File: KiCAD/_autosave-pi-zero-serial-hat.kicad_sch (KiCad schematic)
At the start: 44 parts, among them J1 Conn_02x20_Counter_Clockwise, J2 Conn_01x02_Pin, J4 Screw_Terminal_01x04, Q1 AO3401A, Q2 MMBT5401, Q3 MMBT5401, U1 MAX13487EESA+, U2 TPS5430DDA

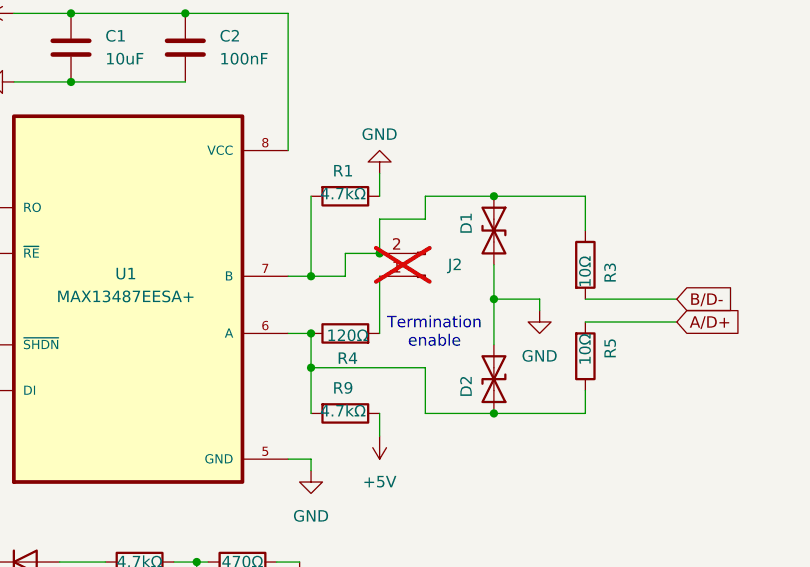
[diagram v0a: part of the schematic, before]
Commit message: Updated layout to fit on a single sided zero form factor board
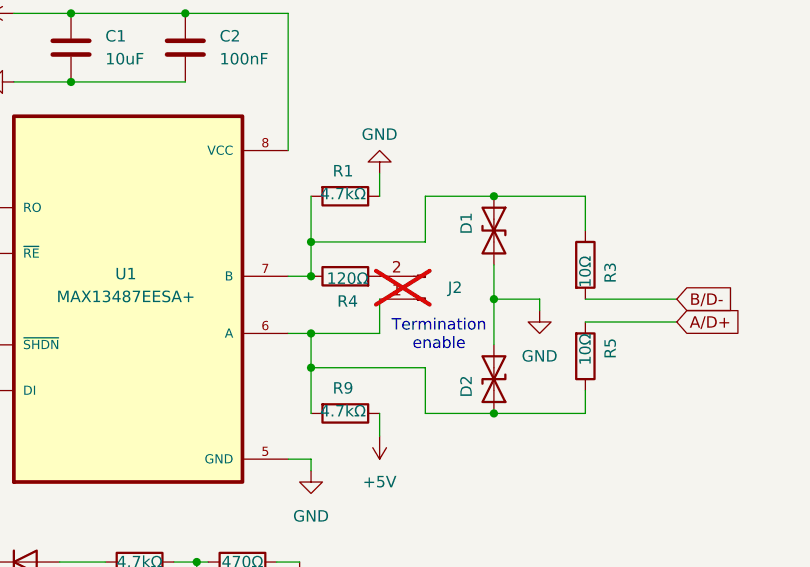
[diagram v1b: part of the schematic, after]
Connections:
- net at J2.1 (Pin_1): now also D2.1 (A1), R5.1, R9.2, U1.6 (A); no longer R4.2
- net at D1.1 (A1), R1.2, R3.1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: now also R4.1; no longer J2.2 (Pin_2)
- new net: J2.2 (Pin_2), R4.2
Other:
- moved on the sheet: J2, R4
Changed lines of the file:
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@@
 	)
 	(junction
-		(at 29.21 127)
-		(diameter 0)
-		(color 0 0 0 0)
-	)
-	(junction
-		(at 106.68 62.23)
+		(at 146.05 45.72)
 		(diameter 0)
 		(color 0 0 0 0)
 	)
 	(junction
-		(at 153.67 46.99)
+		(at 29.21 127)
 		(diameter 0)
 		(color 0 0 0 0)
 	)
 	(junction
-		(at 146.05 55.88)
+		(at 106.68 62.23)
 		(diameter 0)
 		(color 0 0 0 0)
@@
 	)
 	(junction
-		(at 146.05 49.53)
-		(diameter 0)
-		(color 0 0 0 0)
-	)
-	(junction
 		(at 95.25 127)
 		(diameter 0)
@@
 	)
 	(junction
+		(at 146.05 49.53)
+		(diameter 0)
+		(color 0 0 0 0)
+	)
+	(junction
 		(at 107.95 127)
 		(diameter 0)
@@
 		(color 0 0 0 0)
 	)
+	(junction
+		(at 146.05 55.88)
+		(diameter 0)
+		(color 0 0 0 0)
+	)
 	(no_connect
 		(at 43.18 55.88)
@@
 	(wire
 		(pts
-			(xy 149.86 49.53) (xy 149.86 46.99)
-		)
-		(stroke
-			(width 0)
-			(type default)
-		)
-	)
-	(wire
-		(pts
-			(xy 153.67 43.18) (xy 158.75 43.18)
-		)
-		(stroke
-			(width 0)
-			(type default)
-		)
-	)
-	(wire
-		(pts
 			(xy 107.95 127) (xy 107.95 128.27)
 		)
@@
 	(wire
 		(pts
-			(xy 158.75 43.18) (xy 158.75 40.64)
+			(xy 39.37 127) (xy 52.07 127)
 		)
 		(stroke
@@
 	(wire
 		(pts
-			(xy 39.37 127) (xy 52.07 127)
+			(xy 241.3 40.64) (xy 241.3 50.8)
 		)
 		(stroke
@@
 	(wire
 		(pts
-			(xy 241.3 40.64) (xy 241.3 50.8)
+			(xy 158.75 59.69) (xy 158.75 64.77)
 		)
 		(stroke
@@
 	(wire
 		(pts
-			(xy 158.75 59.69) (xy 158.75 64.77)
+			(xy 105.41 41.91) (xy 107.95 41.91)
 		)
 		(stroke
@@
 	(wire
 		(pts
-			(xy 105.41 41.91) (xy 107.95 41.91)
+			(xy 158.75 40.64) (xy 166.37 40.64)
 		)
 		(stroke
@@
 	(wire
 		(pts
-			(xy 158.75 40.64) (xy 166.37 40.64)
+			(xy 146.05 55.88) (xy 153.67 55.88)
 		)
 		(stroke
@@
 	(wire
 		(pts
+			(xy 153.67 52.07) (xy 153.67 55.88)
+		)
+		(stroke
+			(width 0)
+			(type default)
+		)
+	)
+	(wire
+		(pts
 			(xy 166.37 52.07) (xy 171.45 52.07)
 		)
@@
 	(wire
 		(pts
-			(xy 146.05 49.53) (xy 149.86 49.53)
+			(xy 146.05 45.72) (xy 158.75 45.72)
 		)
 		(stroke
@@
 	(wire
 		(pts
-			(xy 146.05 40.64) (xy 146.05 49.53)
-		)
-		(stroke
-			(width 0)
-			(type default)
-		)
-	)
-	(wire
-		(pts
-			(xy 153.67 49.53) (xy 153.67 55.88)
+			(xy 146.05 40.64) (xy 146.05 45.72)
 		)
 		(stroke
@@
 	(wire
 		(pts
-			(xy 149.86 46.99) (xy 153.67 46.99)
+			(xy 97.79 41.91) (xy 96.52 41.91)
 		)
 		(stroke
@@
 	(wire
 		(pts
-			(xy 97.79 41.91) (xy 96.52 41.91)
+			(xy 29.21 127) (xy 39.37 127)
 		)
 		(stroke
@@
 	(wire
 		(pts
-			(xy 29.21 127) (xy 39.37 127)
+			(xy 29.21 137.16) (xy 29.21 139.7)
 		)
 		(stroke
@@
 	(wire
 		(pts
-			(xy 29.21 137.16) (xy 29.21 139.7)
+			(xy 130.81 91.44) (xy 133.35 91.44)
 		)
 		(stroke
@@
 	(wire
 		(pts
-			(xy 130.81 91.44) (xy 133.35 91.44)
+			(xy 113.03 20.32) (xy 119.38 20.32)
 		)
 		(stroke
@@
 	(wire
 		(pts
-			(xy 113.03 20.32) (xy 119.38 20.32)
+			(xy 93.98 62.23) (xy 97.79 62.23)
 		)
 		(stroke
@@
 	(wire
 		(pts
-			(xy 93.98 62.23) (xy 97.79 62.23)
+			(xy 118.11 81.28) (xy 123.19 81.28)
 		)
 		(stroke
@@
 	(wire
 		(pts
-			(xy 118.11 81.28) (xy 123.19 81.28)
+			(xy 158.75 40.64) (xy 158.75 45.72)
 		)
 		(stroke
@@
 	(wire
 		(pts
-			(xy 153.67 46.99) (xy 153.67 43.18)
+			(xy 135.89 127) (xy 151.13 127)
 		)
 		(stroke
@@
 	(wire
 		(pts
-			(xy 135.89 127) (xy 151.13 127)
+			(xy 146.05 45.72) (xy 146.05 49.53)
 		)
 		(stroke
@@
 	(text "Termination\nenable"
 		(exclude_from_sim no)
-		(at 159.766 55.88 0)
+		(at 160.274 56.134 0)
 		(effects
 			(font
@@
 	(symbol
 		(lib_id "Connector:Conn_01x02_Pin")
-		(at 158.75 49.53 180)
+		(at 158.75 52.07 180)
 		(unit 1)
 		(exclude_from_sim no)
@@
 		(dnp yes)
 		(property "Reference" "J2"
-			(at 162.052 48.26 0)
+			(at 162.052 50.8 0)
 			(effects
 				(font
@@
 		)
 		(property "Value" "Conn_01x02_Pin"
-			(at 158.115 52.07 0)
+			(at 158.115 54.61 0)
 			(effects
 				(font
@@
 		)
 		(property "Footprint" "Connector_PinHeader_2.54mm:PinHeader_1x02_P2.54mm_Vertical"
-			(at 158.75 49.53 0)
+			(at 158.75 52.07 0)
 			(effects
 				(font
@@
 		)
 		(property "Datasheet" "~"
-			(at 158.75 49.53 0)
+			(at 158.75 52.07 0)
 			(effects
 				(font
@@
 		)
 		(property "Description" "Generic connector, single row, 01x02, script generated"
-			(at 158.75 49.53 0)
+			(at 158.75 52.07 0)
 			(effects
 				(font
@@
 		)
 		(property "Comment" ""
-			(at 158.75 49.53 0)
+			(at 158.75 52.07 0)
 			(effects
 				(font
@@
 		)
 		(property "Designator" ""
-			(at 158.75 49.53 0)
+			(at 158.75 52.07 0)
 			(effects
 				(font
@@
 		)
 		(property "JLCPCB Part #" ""
-			(at 158.75 49.53 0)
+			(at 158.75 52.07 0)
 			(effects
 				(font
@@
 	(symbol
 		(lib_id "Device:R")
-		(at 149.86 55.88 90)
+		(at 149.86 49.53 90)
 		(unit 1)
 		(exclude_from_sim no)
@@
 		(dnp no)
 		(property "Reference" "R4"
-			(at 150.114 58.674 90)
+			(at 150.114 52.324 90)
 			(effects
 				(font
@@
 		)
 		(property "Value" "120Ω"
-			(at 150.114 56.134 90)
+			(at 150.114 49.784 90)
 			(effects
 				(font
@@
 		)
 		(property "Footprint" "Resistor_SMD:R_0603_1608Metric"
-			(at 149.86 57.658 90)
+			(at 149.86 51.308 90)
 			(effects
 				(font
@@
 		)
 		(property "Datasheet" "~"
-			(at 149.86 55.88 0)
+			(at 149.86 49.53 0)
 			(effects
 				(font
@@
 		)
 		(property "Description" "Resistor"
-			(at 149.86 55.88 0)
+			(at 149.86 49.53 0)
 			(effects
 				(font
@@
 		)
 		(property "Comment" ""
-			(at 149.86 55.88 0)
+			(at 149.86 49.53 0)
 			(effects
 				(font
@@
 		)
 		(property "Designator" ""
-			(at 149.86 55.88 0)
+			(at 149.86 49.53 0)
 			(effects
 				(font
@@
 		)
 		(property "JLCPCB Part #" "C22787"
-			(at 149.86 55.88 0)
+			(at 149.86 49.53 0)
 			(effects
 				(font
